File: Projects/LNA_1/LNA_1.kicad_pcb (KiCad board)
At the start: 2 copper layers, 57.8 x 27.9 mm, 29 parts, among them J1 SMA-J-P-H-ST-EM1, J2 SMA-J-P-H-ST-EM1, Q2 BFR193, U1 BFU790F

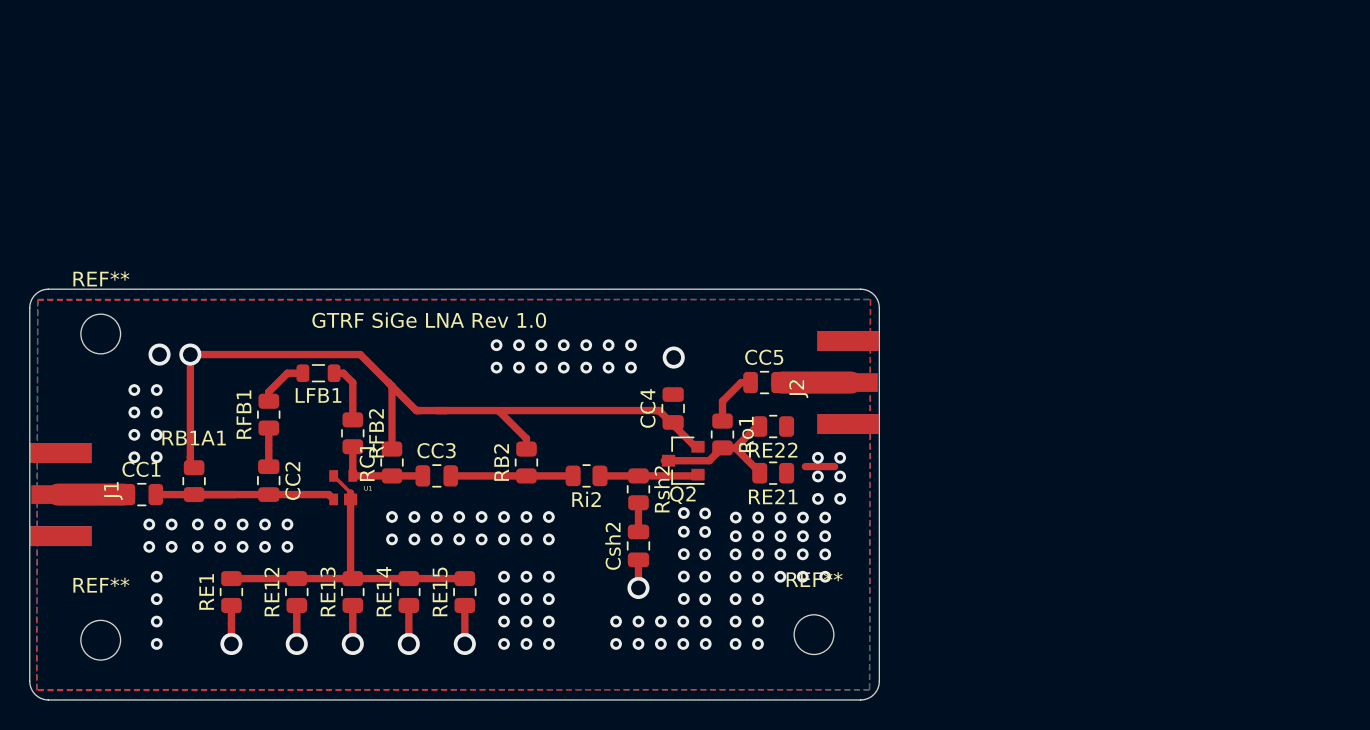
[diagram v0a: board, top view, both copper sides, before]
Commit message: fixed SMA connectors
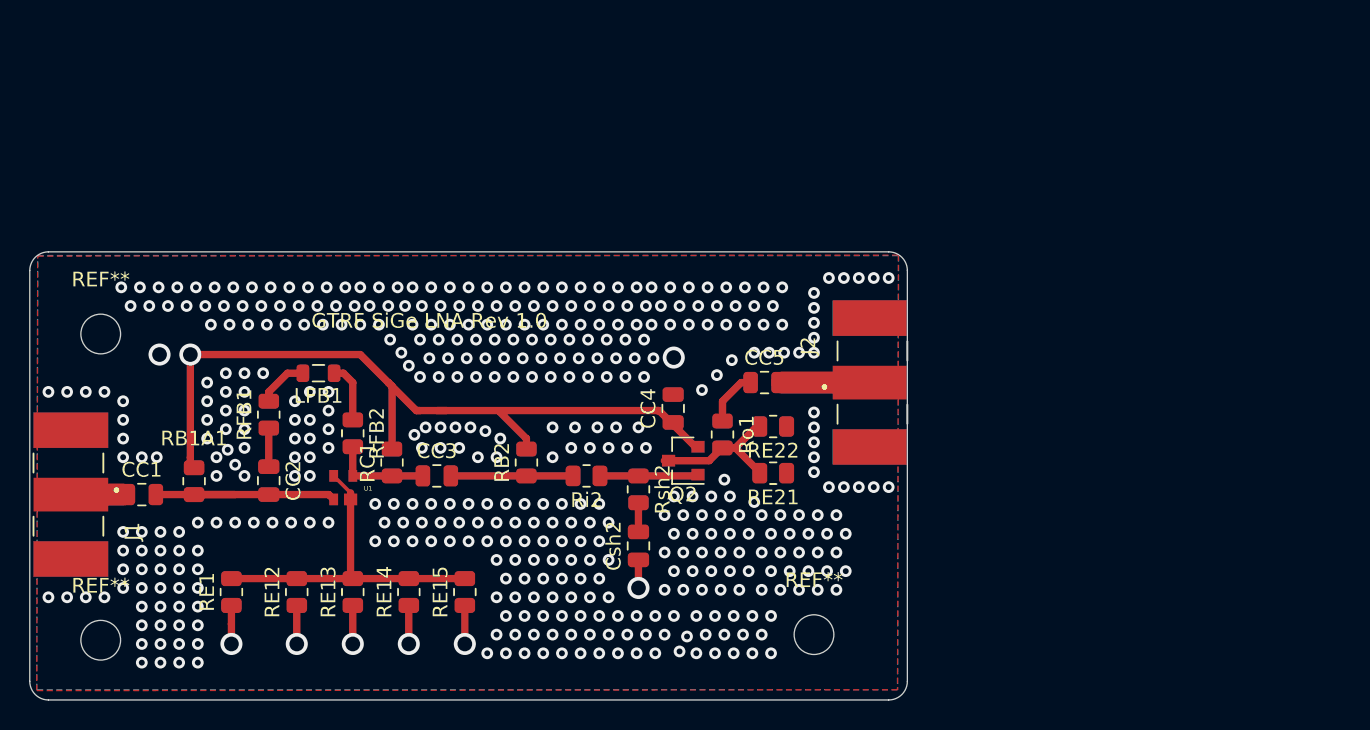
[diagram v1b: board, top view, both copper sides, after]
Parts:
- J1, J2: value SMA-J-P-H-ST-EM1 -> ECE4415PrefferedSMA; footprint SAMTEC_SMA-J-P-H-ST-EM1 -> AdditionalLibs:ECE4415PrefferedSMA
- moved J2 1.27 mm to (138.4, 61.0), turned to 270 degrees
- moved J1 0.89 mm to (84.1, 68.6), turned to 90 degrees
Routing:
- net GND: track 17.0 -> 15.0 mm, vias 128 -> 455
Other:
- board size 57.8 x 27.9 mm -> 59.7 x 30.5 mm

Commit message: added via stitching to the boards and changed to a barrel jack on the LNA
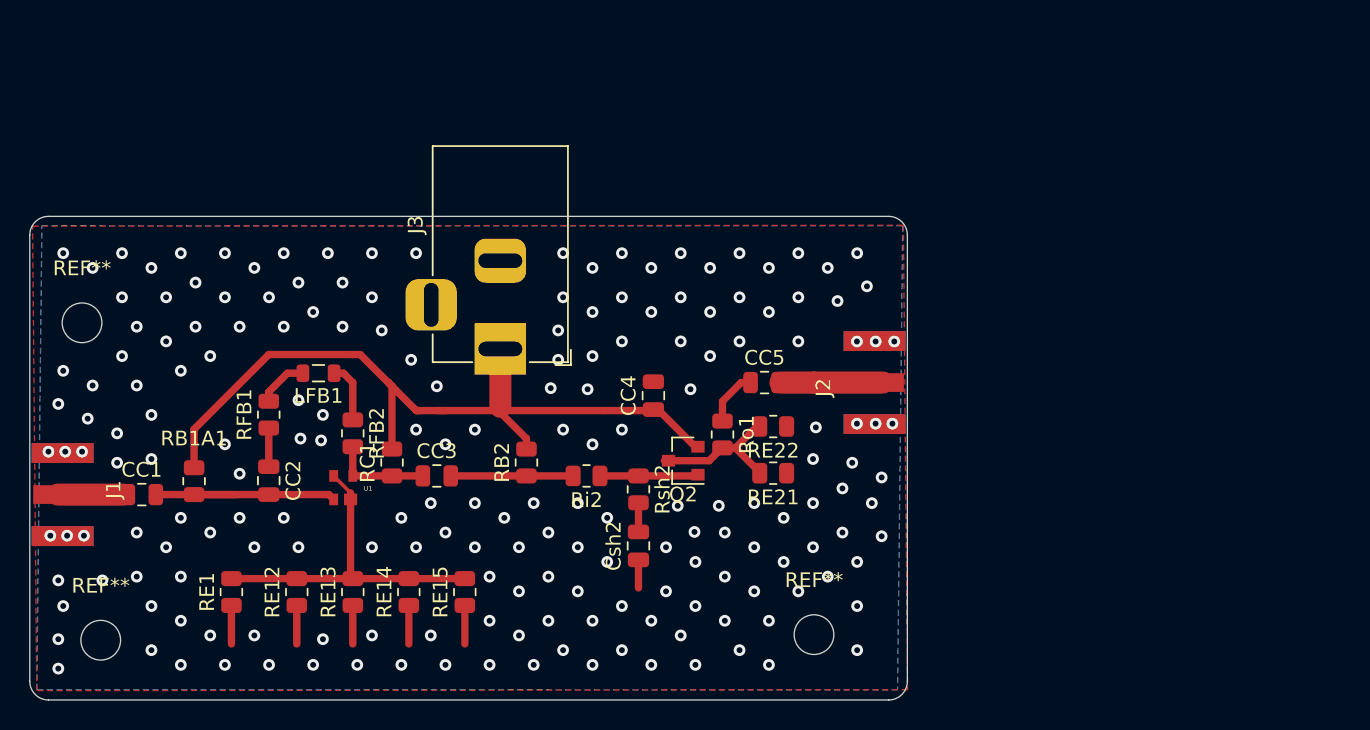
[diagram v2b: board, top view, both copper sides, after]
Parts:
- added J3: Barrel_Jack_MountingPin, Connector_BarrelJack:BarrelJack_Horizontal, F.Cu at (113.3, 58.7)
- J1, J2: value ECE4415PrefferedSMA -> SMA-J-P-H-ST-EM1; footprint AdditionalLibs:ECE4415PrefferedSMA -> AdditionalLibs:SAMTEC_SMA-J-P-H-ST-EM1
- moved CC4 1.60 mm to (123.7, 61.8)
- moved REF** 1.48 mm to (84.8, 56.9)
- moved J1 0.76 mm to (83.3, 68.6), turned to 270 degrees
- moved J2 0.51 mm to (138.9, 61.0), turned to 90 degrees
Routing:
- net Net-(CC5-Pad2): track 4.70 -> 6.98 mm
- net VCC: track 54.2 -> 56.2 mm, vias 1 -> 0
- net GND: vias 455 -> 194
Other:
- board size 59.7 x 30.5 mm -> 59.7 x 32.9 mm
- board text removed: "GTRF SiGe LNA Rev 1.0"

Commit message: fixed the BF193 on the LNA was in wrong orientation
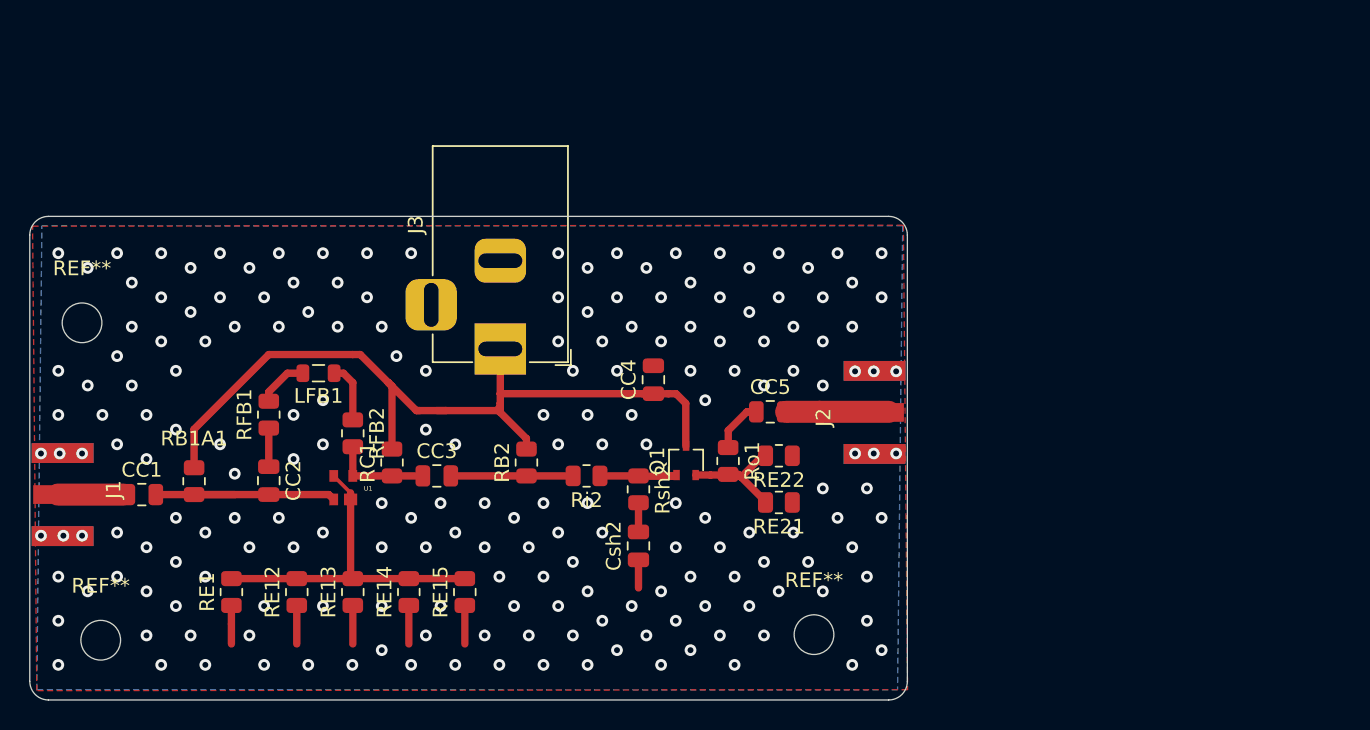
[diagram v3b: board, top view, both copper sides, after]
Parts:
- removed Q2: BFR193, Package_TO_SOT_SMD:SOT-23
- added Q1: Q_NPN_BEC, Package_TO_SOT_SMD:SOT-323_SC-70, F.Cu at (125.9, 66.2)
- moved J2 2.03 mm to (138.9, 63.0)
- moved CC5 2.03 mm to (131.6, 63.0)
- moved RE21 2.03 mm to (132.2, 69.1)
- moved RE22 2.03 mm to (132.2, 65.9)
- moved Ro1 1.84 mm to (128.8, 66.3)
- moved CC4 1.08 mm to (123.7, 60.8)
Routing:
- net Net-(Q1-Pad2): track 9.79 -> 7.71 mm
- net VCC: track 56.2 -> 58.2 mm
- net Net-(Q1-Pad1): track 6.37 -> 7.73 mm
- net GND: vias 194 -> 200

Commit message: added tantalum 10uF cap to the power supply
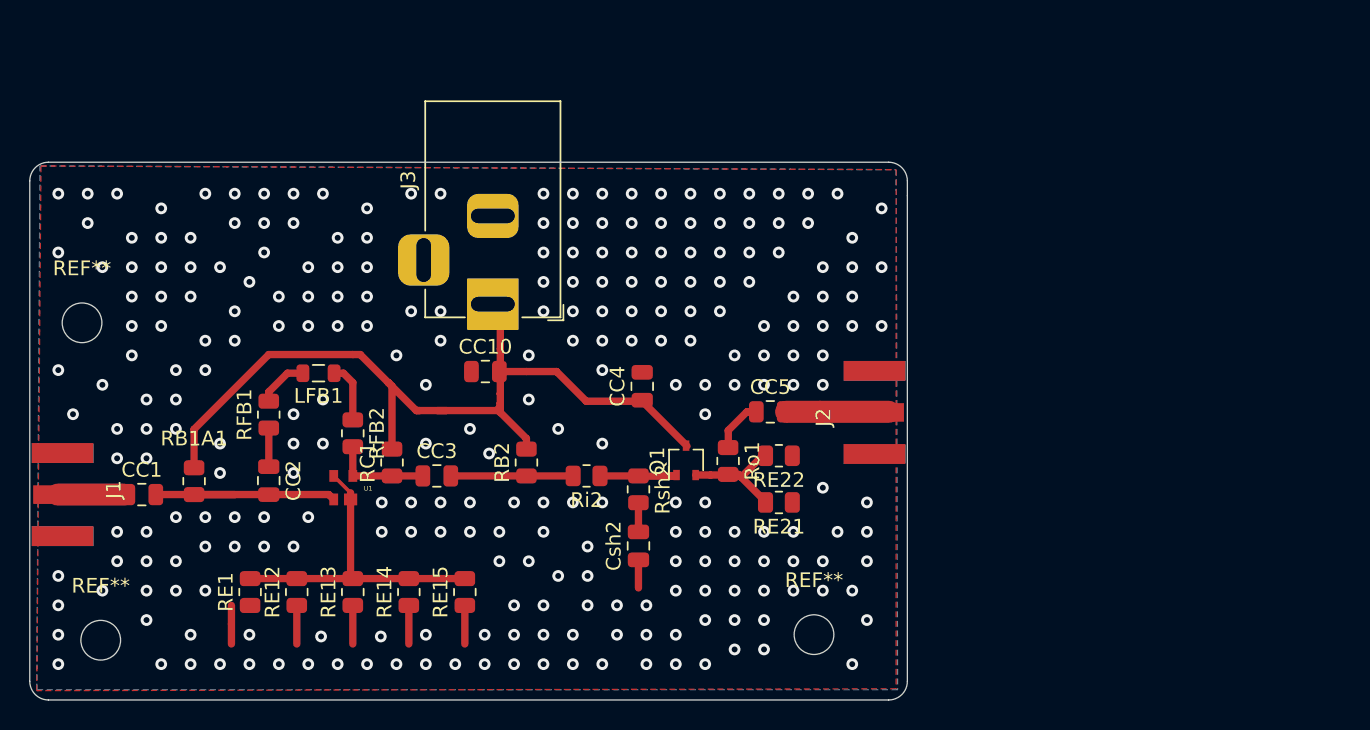
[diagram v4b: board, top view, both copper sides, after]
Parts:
- added CC10: 10u, Capacitor_SMD:C_0805_2012Metric, F.Cu at (112.3, 60.2)
- moved J3 3.09 mm to (112.8, 55.6)
- moved RE1 1.27 mm to (96.3, 75.2)
- moved CC4 0.88 mm to (122.9, 61.2)
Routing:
- net Net-(RE1-Pad2): track 23.4 -> 22.1 mm
- net VCC: track 58.2 -> 58.9 mm
- net GND: vias 200 -> 265
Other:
- board size 59.7 x 32.9 mm -> 59.7 x 36.6 mm

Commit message: Created a new file
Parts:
- CC10: footprint Capacitor_SMD:C_0805_2012Metric -> Capacitor_SMD:C_1206_3216Metric
- moved J3 0.76 mm to (112.8, 54.9)
- moved CC10 0.51 mm to (111.8, 60.2)

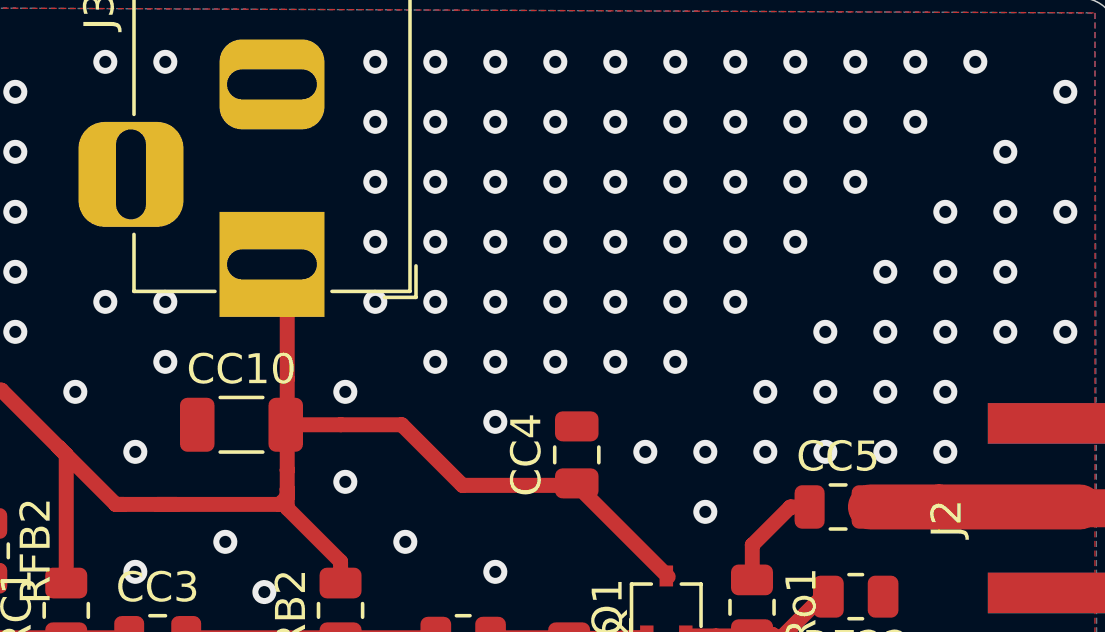
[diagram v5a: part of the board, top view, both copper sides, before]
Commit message: added a demodulation board
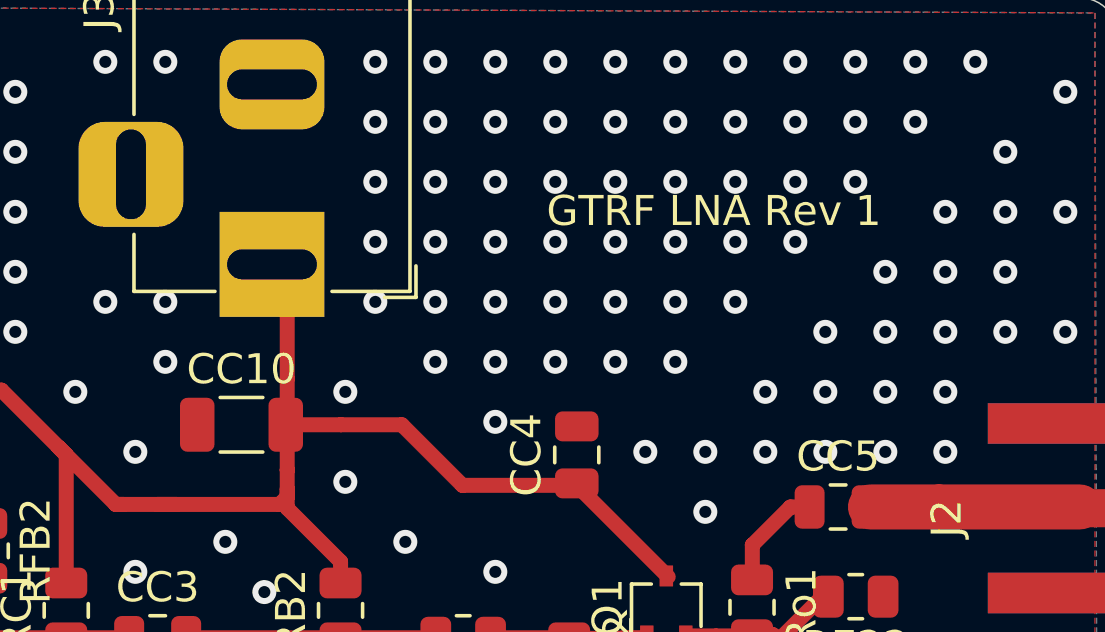
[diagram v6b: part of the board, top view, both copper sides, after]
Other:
- board text added: "GTRF LNA Rev 1"

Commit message: This is the latest version with updated footprints etc
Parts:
- removed the REF** at (134.6, 78.1)
- removed the REF** at (86.1, 78.5)
- added REF**: MountingHole_2.7mm_M2.5, MountingHole:MountingHole_2.7mm_M2.5, F.Cu at (164.1, 76.8)
- added REF**: MountingHole_2.7mm_M2.5, MountingHole:MountingHole_2.7mm_M2.5, F.Cu at (115.6, 77.2)
- moved CC3 29.5 mm to (138.4, 66.0)
- moved J3 29.5 mm to (142.2, 53.6)
- moved RB2 29.5 mm to (144.5, 65.1)
- moved RE15 29.5 mm to (140.3, 73.9)
- moved CC1 29.5 mm to (118.4, 67.3)
- moved CC2 29.5 mm to (127.0, 66.4)
- moved CC4 29.5 mm to (152.4, 59.9)
- moved CC5 29.5 mm to (161.1, 61.7)
- moved J1 29.5 mm to (112.8, 67.3)
- moved J2 29.5 mm to (168.4, 61.7)
- moved LFB1 29.5 mm to (130.4, 59.1)
- moved RB1A1 29.5 mm to (121.9, 66.4)
- moved RC1 29.5 mm to (135.4, 65.1)
- moved RE1 29.5 mm to (125.7, 73.9)
- moved RE12 29.5 mm to (128.9, 73.9)
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
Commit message: post board review they are all ready to order
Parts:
- CC10: footprint Capacitor_SMD:C_1206_3216Metric -> Capacitor_Tantalum_SMD:CP_EIA-6032-28_Kemet-C
- moved J3 2.79 mm to (142.2, 50.8)
- moved CC10 2.63 mm to (140.2, 56.5)
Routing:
- net VCC: track 58.9 -> 61.5 mm
- net GND: vias 265 -> 287
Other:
- board size 59.7 x 36.6 mm -> 59.7 x 41.9 mm
